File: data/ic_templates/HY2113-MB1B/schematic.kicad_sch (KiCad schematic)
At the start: 12 parts, among them J1 B+/B-/P+/P-, Q1 FS8205A, U1 HY2113-MB1B

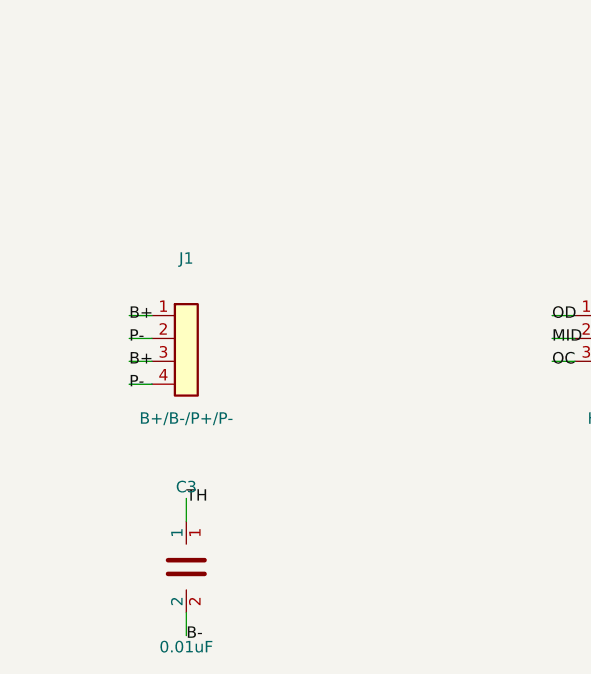
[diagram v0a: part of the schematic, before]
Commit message: fix: 修复黑框检测阈值策略 — 固定阈值70改为 Otsu+Adaptive 混合阈值
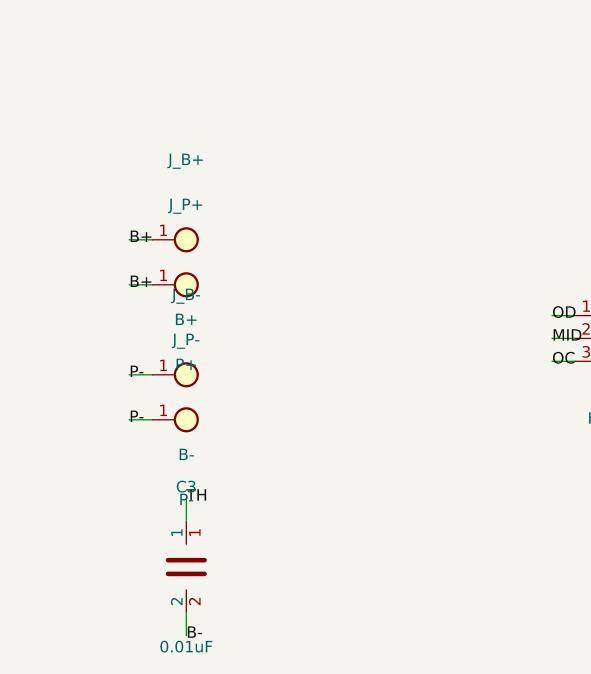
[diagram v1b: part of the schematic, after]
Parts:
- removed J1: B+/B-/P+/P-, Connector_PinHeader_2.54mm:PinHeader_1x04_P2.54mm_Vertical, symbol battery_protection:Conn_01x04
- added J_B+: B+, Connector_PinHeader_2.54mm:PinHeader_1x01_P2.54mm_Vertical, symbol battery_protection:Conn_01x01
- added J_B-: B-, Connector_PinHeader_2.54mm:PinHeader_1x01_P2.54mm_Vertical, symbol battery_protection:Conn_01x01
- added J_P+: P+, Connector_PinHeader_2.54mm:PinHeader_1x01_P2.54mm_Vertical, symbol battery_protection:Conn_01x01
- added J_P-: P-, Connector_PinHeader_2.54mm:PinHeader_1x01_P2.54mm_Vertical, symbol battery_protection:Conn_01x01
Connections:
- net B+: now also J_B+.1, J_P+.1
- net P-: now also J_B-.1, J_P-.1
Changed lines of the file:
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@@
     (comment 1 "Common-port, FS8205A companion")
   )
-  (symbol (lib_id "battery_protection:Conn_01x04") (at 25.4 60.96 0) (unit 1)
-    (exclude_from_sim no) (in_bom yes) (on_board yes) (dnp no)
-    (property "Reference" "J1" (at 25.4 52.07 0)
-      (effects (font (size 1.27 1.27))))
-    (property "Value" "B+/B-/P+/P-" (at 25.4 69.85 0)
-      (effects (font (size 1.27 1.27))))
-    (property "Footprint" "Connector_PinHeader_2.54mm:PinHeader_1x04_P2.54mm_Vertical" (at 0 0 0)
-      (effects (font (size 1.27 1.27)) hide))
-    (property "Datasheet" "" (at 0 0 0)
-      (effects (font (size 1.27 1.27)) hide))
-    (instances
-      (project "template" (path "/0dc5b4e4-560f-4eb4-9c36-caee4f454450" (reference "J1") (unit 1))))
-    (pin "1")
-    (pin "2")
-    (pin "3")
-    (pin "4")
+  (symbol (lib_id "battery_protection:Conn_01x01") (at 25.4 50.0 0) (unit 1)
+    (exclude_from_sim no) (in_bom yes) (on_board yes) (dnp no)
+    (property "Reference" "J_B+" (at 25.4 41.11 0)
+      (effects (font (size 1.27 1.27))))
+    (property "Value" "B+" (at 25.4 58.89 0)
+      (effects (font (size 1.27 1.27))))
+    (property "Footprint" "Connector_PinHeader_2.54mm:PinHeader_1x01_P2.54mm_Vertical" (at 0 0 0)
+      (effects (font (size 1.27 1.27)) hide))
+    (property "Datasheet" "" (at 0 0 0)
+      (effects (font (size 1.27 1.27)) hide))
+    (instances
+      (project "template" (path "/631c56ff-3dd5-47b9-ac31-a1e5363bc13a" (reference "J_B+") (unit 1))))
+    (pin "1")
+  )
+  (symbol (lib_id "battery_protection:Conn_01x01") (at 25.4 55.0 0) (unit 1)
+    (exclude_from_sim no) (in_bom yes) (on_board yes) (dnp no)
+    (property "Reference" "J_P+" (at 25.4 46.11 0)
+      (effects (font (size 1.27 1.27))))
+    (property "Value" "P+" (at 25.4 63.89 0)
+      (effects (font (size 1.27 1.27))))
+    (property "Footprint" "Connector_PinHeader_2.54mm:PinHeader_1x01_P2.54mm_Vertical" (at 0 0 0)
+      (effects (font (size 1.27 1.27)) hide))
+    (property "Datasheet" "" (at 0 0 0)
+      (effects (font (size 1.27 1.27)) hide))
+    (instances
+      (project "template" (path "/48960b14-c19c-4482-b106-dda5dcfa06ce" (reference "J_P+") (unit 1))))
+    (pin "1")
+  )
+  (symbol (lib_id "battery_protection:Conn_01x01") (at 25.4 65.0 0) (unit 1)
+    (exclude_from_sim no) (in_bom yes) (on_board yes) (dnp no)
+    (property "Reference" "J_B-" (at 25.4 56.11 0)
+      (effects (font (size 1.27 1.27))))
+    (property "Value" "B-" (at 25.4 73.89 0)
+      (effects (font (size 1.27 1.27))))
+    (property "Footprint" "Connector_PinHeader_2.54mm:PinHeader_1x01_P2.54mm_Vertical" (at 0 0 0)
+      (effects (font (size 1.27 1.27)) hide))
+    (property "Datasheet" "" (at 0 0 0)
+      (effects (font (size 1.27 1.27)) hide))
+    (instances
+      (project "template" (path "/65307397-913e-4c3f-9128-38d219b63ff0" (reference "J_B-") (unit 1))))
+    (pin "1")
+  )
+  (symbol (lib_id "battery_protection:Conn_01x01") (at 25.4 70.0 0) (unit 1)
+    (exclude_from_sim no) (in_bom yes) (on_board yes) (dnp no)
+    (property "Reference" "J_P-" (at 25.4 61.11 0)
+      (effects (font (size 1.27 1.27))))
+    (property "Value" "P-" (at 25.4 78.89 0)
+      (effects (font (size 1.27 1.27))))
+    (property "Footprint" "Connector_PinHeader_2.54mm:PinHeader_1x01_P2.54mm_Vertical" (at 0 0 0)
+      (effects (font (size 1.27 1.27)) hide))
+    (property "Datasheet" "" (at 0 0 0)
+      (effects (font (size 1.27 1.27)) hide))
+    (instances
+      (project "template" (path "/f27f381f-b905-4e6d-a0e7-2f4122ad4440" (reference "J_P-") (unit 1))))
+    (pin "1")
   )
   (symbol (lib_id "battery_protection:HY2113-MB1B") (at 76.2 60.96 0) (unit 1)
@@
       (effects (font (size 1.27 1.27)) hide))
     (instances
-      (project "template" (path "/fe589668-785f-4f98-92ef-7cf907f6aa54" (reference "U1") (unit 1))))
+      (project "template" (path "/dba0639c-67b7-4340-9075-dec0ee38df17" (reference "U1") (unit 1))))
     (pin "1")
     (pin "2")
@@
       (effects (font (size 1.27 1.27)) hide))
     (instances
-      (project "template" (path "/9f874abd-4c7f-4af7-9625-0a402e9f41ef" (reference "Q1") (unit 1))))
+      (project "template" (path "/4faa4468-6458-438f-bfc1-71a81550aae8" (reference "Q1") (unit 1))))
     (pin "1")
     (pin "2")
@@
       (effects (font (size 1.27 1.27)) hide))
     (instances
-      (project "template" (path "/06feb3b9-f301-4484-be9a-a5a693f666b3" (reference "R1") (unit 1))))
+      (project "template" (path "/61604a9e-c012-4e69-af8b-ee6606cca167" (reference "R1") (unit 1))))
     (pin "1")
     (pin "2")
@@
       (effects (font (size 1.27 1.27)) hide))
     (instances
-      (project "template" (path "/5a21a4a6-3ddb-4ea8-8861-8420082b5864" (reference "R2") (unit 1))))
+      (project "template" (path "/f5193f93-7eac-40d1-bbf1-ceaa7969379c" (reference "R2") (unit 1))))
     (pin "1")
     (pin "2")
@@
       (effects (font (size 1.27 1.27)) hide))
     (instances
-      (project "template" (path "/afcec254-155d-434d-9e5e-82769a7337c6" (reference "R3") (unit 1))))
+      (project "template" (path "/d70b025a-c891-49e2-b6d8-db13bf8c0c3b" (reference "R3") (unit 1))))
     (pin "1")
     (pin "2")
@@
       (effects (font (size 1.27 1.27)) hide))
     (instances
-      (project "template" (path "/3c581808-5c61-4eb1-8b4d-c9f302f2d9e4" (reference "R4") (unit 1))))
+      (project "template" (path "/64180ea8-da03-4330-b466-5d59d0a6107e" (reference "R4") (unit 1))))
     (pin "1")
     (pin "2")
@@
       (effects (font (size 1.27 1.27)) hide))
     (instances
-      (project "template" (path "/39714342-c16c-479d-90f6-27ad2b90af06" (reference "C1") (unit 1))))
+      (project "template" (path "/55dd2c8a-86b3-4239-88a3-4cd0a10bd163" (reference "C1") (unit 1))))
     (pin "1")
     (pin "2")
@@
       (effects (font (size 1.27 1.27)) hide))
     (instances
-      (project "template" (path "/5ceea8b1-2886-4351-ab01-b64374852747" (reference "C2") (unit 1))))
+      (project "template" (path "/b0d69e81-b054-461f-a47b-78964e55add9" (reference "C2") (unit 1))))
     (pin "1")
     (pin "2")
@@
       (effects (font (size 1.27 1.27)) hide))
     (instances
-      (project "template" (path "/169d2066-783e-4bec-afe2-2a30f72ba7ab" (reference "C3") (unit 1))))
+      (project "template" (path "/0e7b4d73-5115-49a6-a93d-8cb3dccf35c9" (reference "C3") (unit 1))))
     (pin "1")
     (pin "2")
@@
       (effects (font (size 1.27 1.27)) hide))
     (instances
-      (project "template" (path "/6c0f1dbc-34b1-45a6-9bd1-a36bf824d2a4" (reference "TP_TH") (unit 1))))
+      (project "template" (path "/af340afa-a5fa-41b9-a718-1e2ee305700e" (reference "TP_TH") (unit 1))))
     (pin "1")
   )
@@
       (effects (font (size 1.27 1.27)) hide))
     (instances
-      (project "template" (path "/a066c7fc-b946-4abd-b3d3-405798e547e4" (reference "TP_ID") (unit 1))))
-    (pin "1")
-  )
-  (wire (pts (xy 21.59 58.42) (xy 19.05 58.42))
-    (stroke (width 0) (type default))
-)
-  (label "B+" (at 19.05 58.42 0) (fields_autoplaced yes)
-    (effects (font (size 1.27 1.27)) (justify left))
-)
-  (wire (pts (xy 21.59 60.96) (xy 19.05 60.96))
-    (stroke (width 0) (type default))
-)
-  (label "P-" (at 19.05 60.96 0) (fields_autoplaced yes)
-    (effects (font (size 1.27 1.27)) (justify left))
-)
-  (wire (pts (xy 21.59 63.5) (xy 19.05 63.5))
-    (stroke (width 0) (type default))
-)
-  (label "B+" (at 19.05 63.5 0) (fields_autoplaced yes)
-    (effects (font (size 1.27 1.27)) (justify left))
-)
-  (wire (pts (xy 21.59 66.04) (xy 19.05 66.04))
-    (stroke (width 0) (type default))
-)
-  (label "P-" (at 19.05 66.04 0) (fields_autoplaced yes)
-    (effects (font (size 1.27 1.27)) (justify left))
-)
+      (project "template" (path "/cdc9e572-7c0d-4f4b-8c8c-70b8377c0ec6" (reference "TP_ID") (unit 1))))
+    (pin "1")
+  )
+  (wire (pts (xy 21.59 50.0) (xy 19.05 50.0))
+    (stroke (width 0) (type default))
+)
+  (label "B+" (at 19.05 50.0 0) (fields_autoplaced yes)
+    (effects (font (size 1.27 1.27)) (justify left))
+)
+  (wire (pts (xy 21.59 55.0) (xy 19.05 55.0))
+    (stroke (width 0) (type default))
+)
+  (label "B+" (at 19.05 55.0 0) (fields_autoplaced yes)
+    (effects (font (size 1.27 1.27)) (justify left))
+)
+  (wire (pts (xy 21.59 65.0) (xy 19.05 65.0))
+    (stroke (width 0) (type default))
+)
+  (label "P-" (at 19.05 65.0 0) (fields_autoplaced yes)
+    (effects (font (size 1.27 1.27)) (justify left))
+)
+  (wire (pts (xy 21.59 70.0) (xy 19.05 70.0))
+    (stroke (width 0) (type default))
+)
+  (label "P-" (at 19.05 70.0 0) (fields_autoplaced yes)
+    (effects (font (size 1.27 1.27)) (justify left))
+)
